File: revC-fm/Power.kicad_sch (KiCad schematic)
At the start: 65 parts, among them P2 TSM-102-01-L-SV-P-TR, Q1 MMDT5551-7-F, Q2 MMDT5551-7-F, SW3 SW_SPST, SW4 SW_SPST, SW5 SW_SPST, SW6 SW_SPST, U10 INA226A, U12 TPS54226PWPR, U13 BQ25883RGER, U14 INA226A, U15 INA226A, U43 INA226A, U45 INA226A, U9 ADM1176-1ARMZ-R7

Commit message: routing
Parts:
- removed C44: 3.3nF, Capacitor_SMD:C_0402_1005Metric, symbol Device:C
- removed C57: 0.1uF, Capacitor_SMD:C_0402_1005Metric, symbol Device:C
- removed R32: 1k, Resistor_SMD:R_0603_1608Metric, symbol Device:R_US
- removed R33: 150k, Resistor_SMD:R_0603_1608Metric, symbol Device:R_US
- removed R53: 10mR, SierraLobo:KRL3216, symbol SierraLobo:R_US_SENSE
- removed U15: INA226A, Package_SO:VSSOP-10_3x3mm_P0.5mm, symbol SierraLobo:INA226A
- removed U9: ADM1176-1ARMZ-R7, SierraLobo:ADM1176-1ARMZ-R7, symbol SierraLobo:ADM1176-1ARMZ-R7
- added C60: 0.1uF, Capacitor_SMD:C_0603_1608Metric, symbol Device:C
- added R73, R74: R_US, Resistor_SMD:R_0603_1608Metric, symbol Device:R_US
- added U17: INA230AIRGTR, Package_DFN_QFN:VQFN-16-1EP_3x3mm_P0.5mm_EP1.68x1.68mm, symbol SierraLobo:INA230AxRGT
- C37: renamed from C132; footprint Capacitor_SMD:C_0402_1005Metric -> Capacitor_SMD:C_0603_1608Metric
- C38: renamed from C45; footprint Capacitor_SMD:C_0402_1005Metric -> Capacitor_SMD:C_0603_1608Metric
- C39: renamed from C56; footprint Capacitor_SMD:C_0402_1005Metric -> Capacitor_SMD:C_0603_1608Metric
- C40: renamed from C46; footprint Capacitor_SMD:C_0402_1005Metric -> Capacitor_SMD:C_0603_1608Metric
- C50: renamed from C42; footprint Capacitor_SMD:C_0402_1005Metric -> Capacitor_SMD:C_0603_1608Metric
- C51: renamed from C47; footprint Capacitor_SMD:C_0402_1005Metric -> Capacitor_SMD:C_0603_1608Metric
- C57: renamed from C52; footprint Capacitor_SMD:C_0402_1005Metric -> Capacitor_SMD:C_0603_1608Metric
- R30: renamed from R73; footprint SierraLobo:KRL3216 -> Resistor_SMD:R_1210_3225Metric; symbol SierraLobo:R_US_SENSE -> Device:R_US
- R32: renamed from R52; footprint SierraLobo:KRL3216 -> Resistor_SMD:R_1210_3225Metric; symbol SierraLobo:R_US_SENSE -> Device:R_US
- R50: renamed from R31; value 47mR -> 10mR; footprint SierraLobo:KRL3216 -> Resistor_SMD:R_1210_3225Metric; symbol SierraLobo:R_US_SENSE -> Device:R_US
- U10: renamed from U43; value INA226A -> INA230AIRGTR; footprint Package_SO:VSSOP-10_3x3mm_P0.5mm -> Package_DFN_QFN:VQFN-16-1EP_3x3mm_P0.5mm_EP1.68x1.68mm; symbol SierraLobo:INA226A -> SierraLobo:INA230AxRGT
- U11: renamed from U45; value INA226A -> INA230AIRGTR; footprint Package_SO:VSSOP-10_3x3mm_P0.5mm -> Package_DFN_QFN:VQFN-16-1EP_3x3mm_P0.5mm_EP1.68x1.68mm; symbol SierraLobo:INA226A -> SierraLobo:INA230AxRGT
- U12: renamed from U14; value INA226A -> INA230AIRGTR; footprint Package_SO:VSSOP-10_3x3mm_P0.5mm -> Package_DFN_QFN:VQFN-16-1EP_3x3mm_P0.5mm_EP1.68x1.68mm; symbol SierraLobo:INA226A -> SierraLobo:INA230AxRGT
- U13: renamed from U10; value INA226A -> INA230AIRGTR; footprint Package_SO:VSSOP-10_3x3mm_P0.5mm -> Package_DFN_QFN:VQFN-16-1EP_3x3mm_P0.5mm_EP1.68x1.68mm; symbol SierraLobo:INA226A -> SierraLobo:INA230AxRGT
- renumbered C43 to C42, C49 to C43, C51 to C44, C41 to C45, C37 to C46, C39 to C47, C53 to C48, C55 to C49, C54 to C52, C36 to C53, C38 to C54, C48 to C58, C50 to C59, L3 to L2, L2 to L3, R34 to R31, R35 to R33, R39 to R35, R40 to R36, R42 to R37, R43 to R38, R46 to R39, R41 to R40, R263 to R41, R48 to R42, R47 to R43, R49 to R44, R44 to R45, R45 to R46, R50 to R47, R51 to R48, R54 to R49, R30 to R51, SW5 to SW4, SW4 to SW5, U13 to U15, U12 to U16
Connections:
- net +5V: now also U10.11 (Vbus), U10.12 (Vin-); no longer C43.2, R41.2, R44.1, U15.23 (VBUS)
- net +BATT: now also U11.11 (Vbus); no longer U13.8 (Vbus)
- net 3.3V: now also U10.9 (VS), U11.9 (VS), U12.9 (VS), U13.9 (VS), C60.1, U17.11 (Vbus), U17.12 (Vin-), U17.9 (VS); no longer U10.6 (VS), U11.6 (VS), U12.6 (VS), U13.6 (VS)
- net 3.3Vout: now also U17.13 (Vin+)
- net 5V_BUS_SEN_HI: now also U10.13 (Vin+); no longer U10.8 (Vbus)
- net 5V_PYLD_SEN_HI: now also U12.13 (Vin+); no longer U12.8 (Vbus)
- net SCL_PWR: now also U17.5 (SCL)
- net SDA_PWR: now also U17.4 (SDA)
- net VBUS_PREINHIB: now also U13.11 (Vbus)
- net VCHRG: no longer U11.8 (Vbus)
- net at R33.3: now also U13.12 (Vin-); no longer U13.9 (Vin-)
- net at R33.4: now also U13.13 (Vin+); no longer U13.10 (Vin+)
- net at R31.3: now also U11.12 (Vin-); no longer U11.9 (Vin-)
- net at R31.4: now also U11.13 (Vin+); no longer U11.10 (Vin+)
- net EP: now reaches U12.10 (GND)
- net EP: now also C37.2, C38.2, C39.2, C40.2, C45.1, C46.1, C47.1, C51.2, C53.2, C54.2, C58.2, C70.2, C70.2, Q1.1 (E1), Q1.4 (E2), Q2.1 (E1), Q2.4 (E2), R46.1, R51.2, U10.10 (GND), U10.17 (EP), U11.10 (GND), U11.17 (EP), U12.17 (EP), U13.10 (GND), U13.17 (EP), U16.15 (EPAD), U16.5 (GND), U16.8 (PGND1), U16.9 (PGND2), C60.2, R73.2, R74.2, U17.10 (GND), U17.17 (EP); no longer R32.4
- net 5V_PYLD renamed 5V_PL
- net 5V_PL: now also U12.11 (Vbus), U12.12 (Vin-)
- removed net GND: C37.2, C38.2, C39.2, C40.2, C45.1, C46.1, C47.1, C51.2, C53.2, C54.2, C58.2, C70.2, C70.2, Q1.1 (E1), Q1.4 (E2), Q2.1 (E1), Q2.4 (E2), R46.1, R51.2, U10.7 (GND), U11.7 (GND), U12.7 (GND), U13.7 (GND), U16.15 (EPAD), U16.5 (GND), U16.8 (PGND1), U16.9 (PGND2)
- new net 5V Bus Regulator/LIMIT: R74.1
- new net 5V Payload Regulator/LIMIT: R73.1
- new net 5VUSB: C43.2, R41.2, R44.1, U15.23 (VBUS)
- no-connect marks 9 -> 8
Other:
- removed sheet 5V RF Regulator
- sheet 5V Bus Regulator ports: added LATCH, LIMIT, ~{ALERT}; removed none
- sheet 5V Payload Regulator ports: added LATCH, LIMIT, ~{ALERT}; removed none
- note removed: "5V Power Monitors"
- note removed: "Addr: 0x44"
- moved on the sheet: C37, C38, C39, C40, C42, C43, C44, C45, C46, C47, C48, C49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

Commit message: fm layout
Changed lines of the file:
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@@
     (effects (font (size 1.27 1.27)) (justify left bottom))
   )
-  (text "Charge Power Monitor" (at 92.71 21.59 0)
+  (text "Charge Power Monitor" (at 92.71 17.78 0)
     (effects (font (size 2.159 2.159)) (justify left bottom))
   )

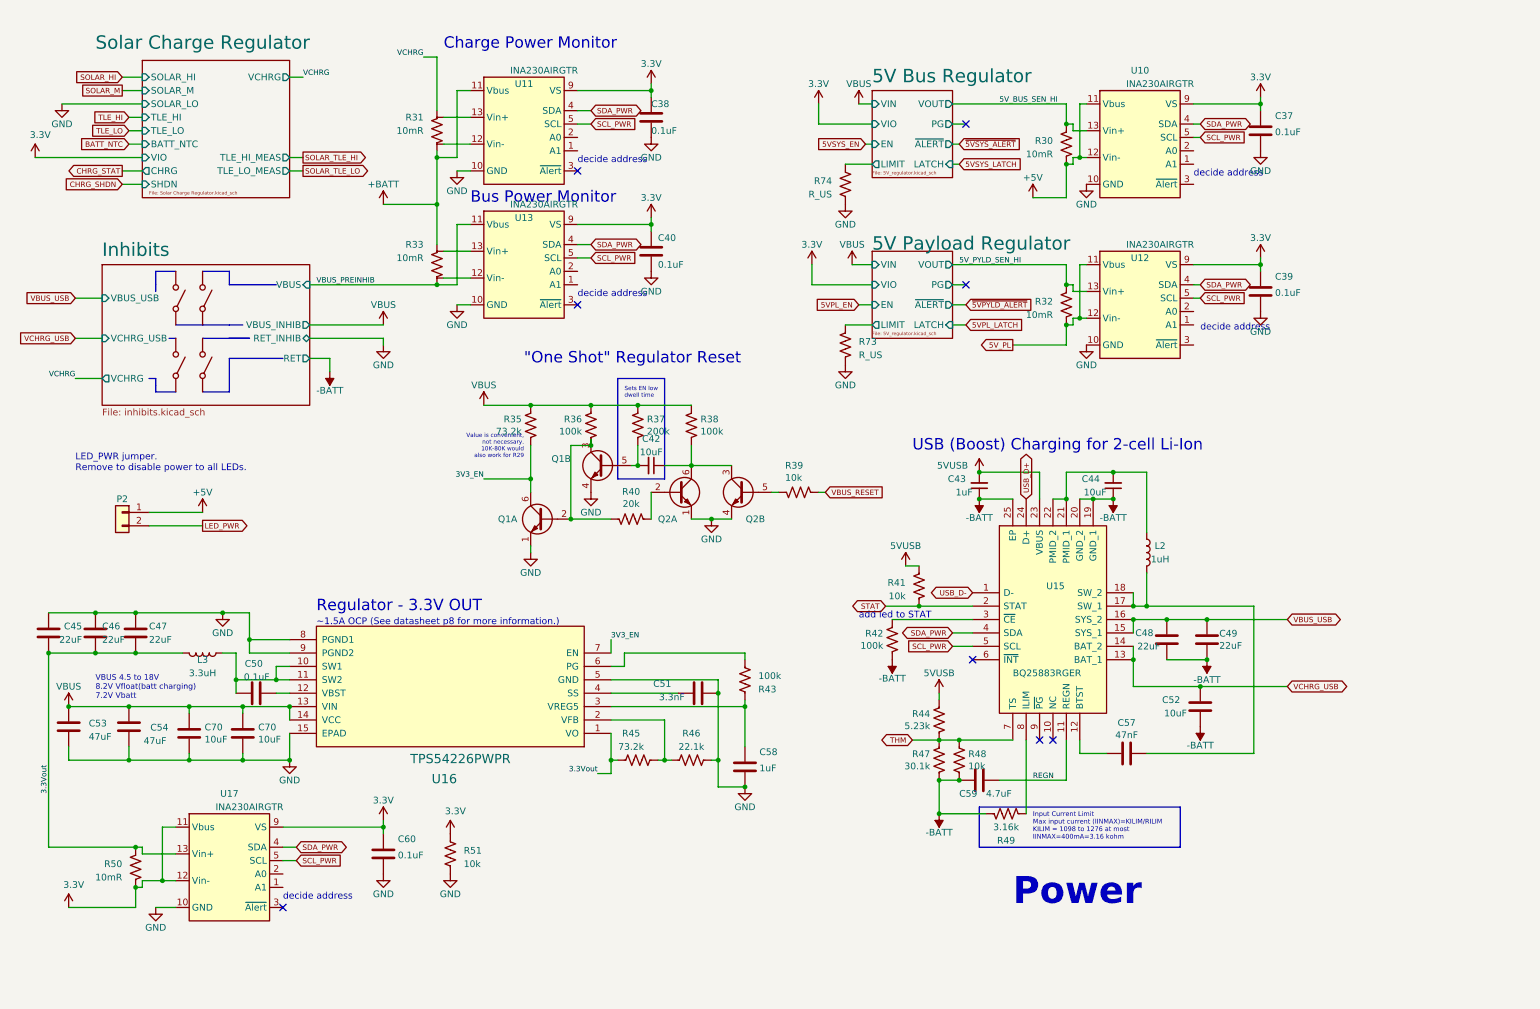
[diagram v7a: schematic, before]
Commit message: changed RF connector to TH
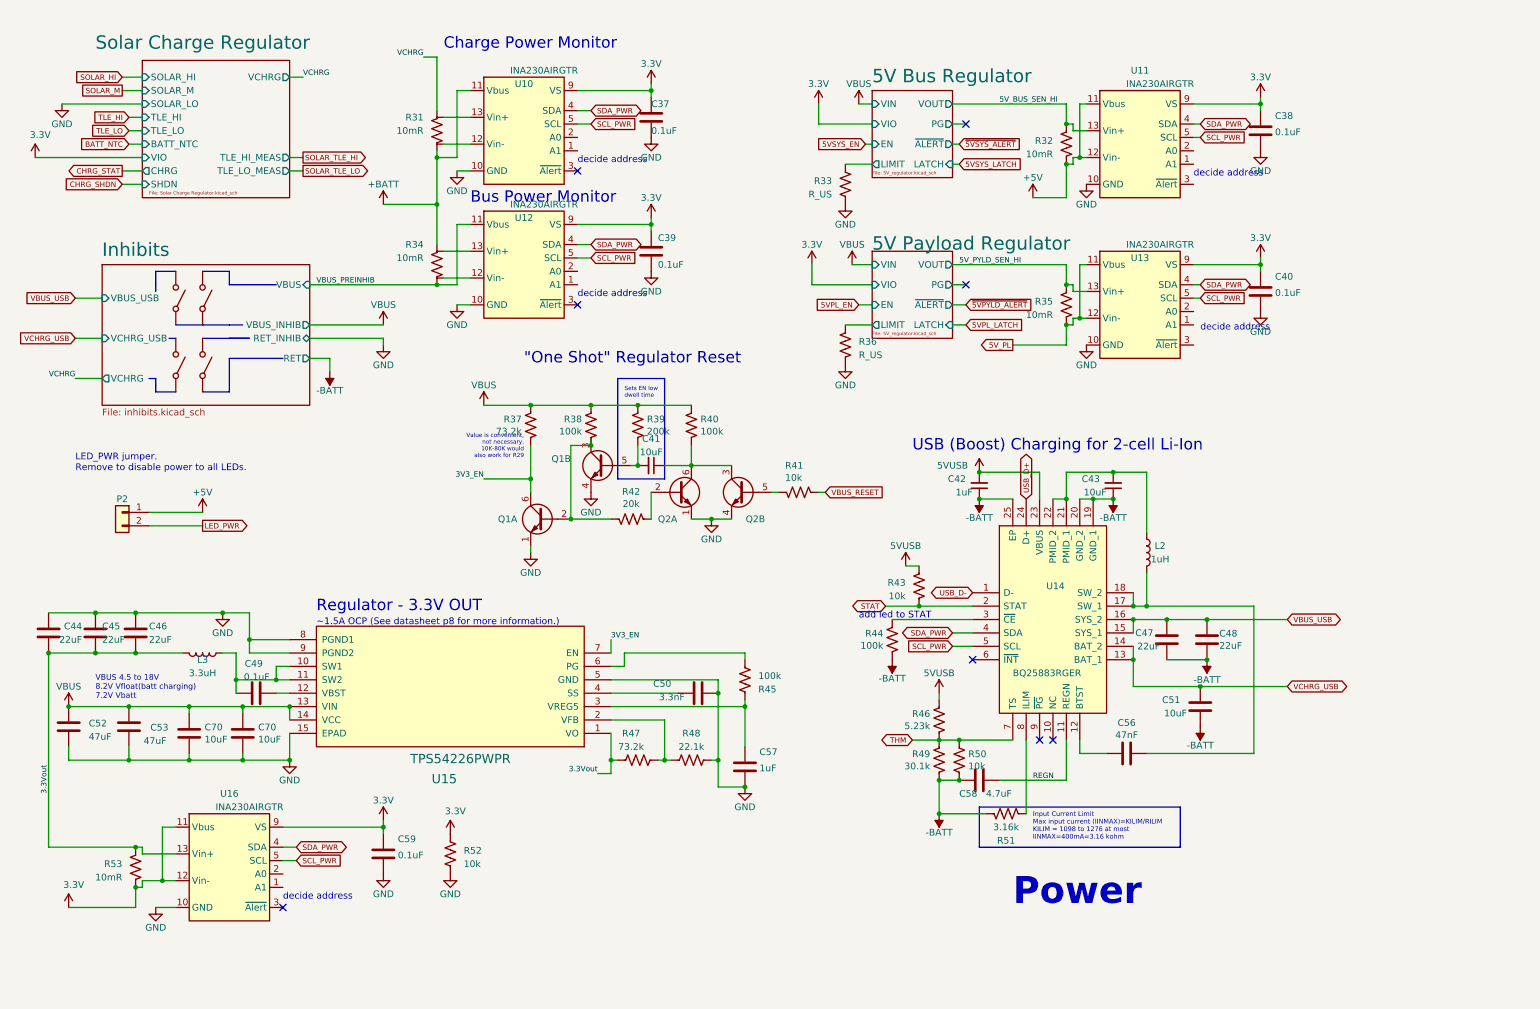
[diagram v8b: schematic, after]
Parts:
- L3: footprint Inductor_SMD:L_Wuerth_HCI-5040 -> SierraLobo:L_Wuerth_HCI-5040
- U10: renamed from U11; footprint Package_DFN_QFN:VQFN-16-1EP_3x3mm_P0.5mm_EP1.68x1.68mm -> SierraLobo:INA230AIRGTR
- U11: renamed from U10; footprint Package_DFN_QFN:VQFN-16-1EP_3x3mm_P0.5mm_EP1.68x1.68mm -> SierraLobo:INA230AIRGTR
- U12: renamed from U13; footprint Package_DFN_QFN:VQFN-16-1EP_3x3mm_P0.5mm_EP1.68x1.68mm -> SierraLobo:INA230AIRGTR
- U13: renamed from U12; footprint Package_DFN_QFN:VQFN-16-1EP_3x3mm_P0.5mm_EP1.68x1.68mm -> SierraLobo:INA230AIRGTR
- U16: renamed from U17; footprint Package_DFN_QFN:VQFN-16-1EP_3x3mm_P0.5mm_EP1.68x1.68mm -> SierraLobo:INA230AIRGTR
- renumbered C38 to C37, C37 to C38, C40 to C39, C39 to C40, C42 to C41, C43 to C42, C44 to C43, C45 to C44, C46 to C45, C47 to C46, C48 to C47, C49 to C48, C50 to C49, C51 to C50, C52 to C51, C53 to C52, C54 to C53, C57 to C56, C58 to C57, C59 to C58, C60 to C59, R30 to R32, R74 to R33, R33 to R34, R32 to R35, R73 to R36, R35 to R37, R36 to R38, R37 to R39, R38 to R40, R39 to R41, R40 to R42, R41 to R43, R42 to R44, R43 to R45, R44 to R46, R45 to R47, R46 to R48, R47 to R49, R48 to R50, R49 to R51, R51 to R52, R50 to R53, U15 to U14, U16 to U15
